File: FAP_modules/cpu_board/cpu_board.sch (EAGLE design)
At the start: 35 parts, among them IC2 74HC245DW, IC3 74HC245DW, IC4 74HC04D, IC7 74HC245DW, IC8 74HC245DW, IC9 74HC245DW

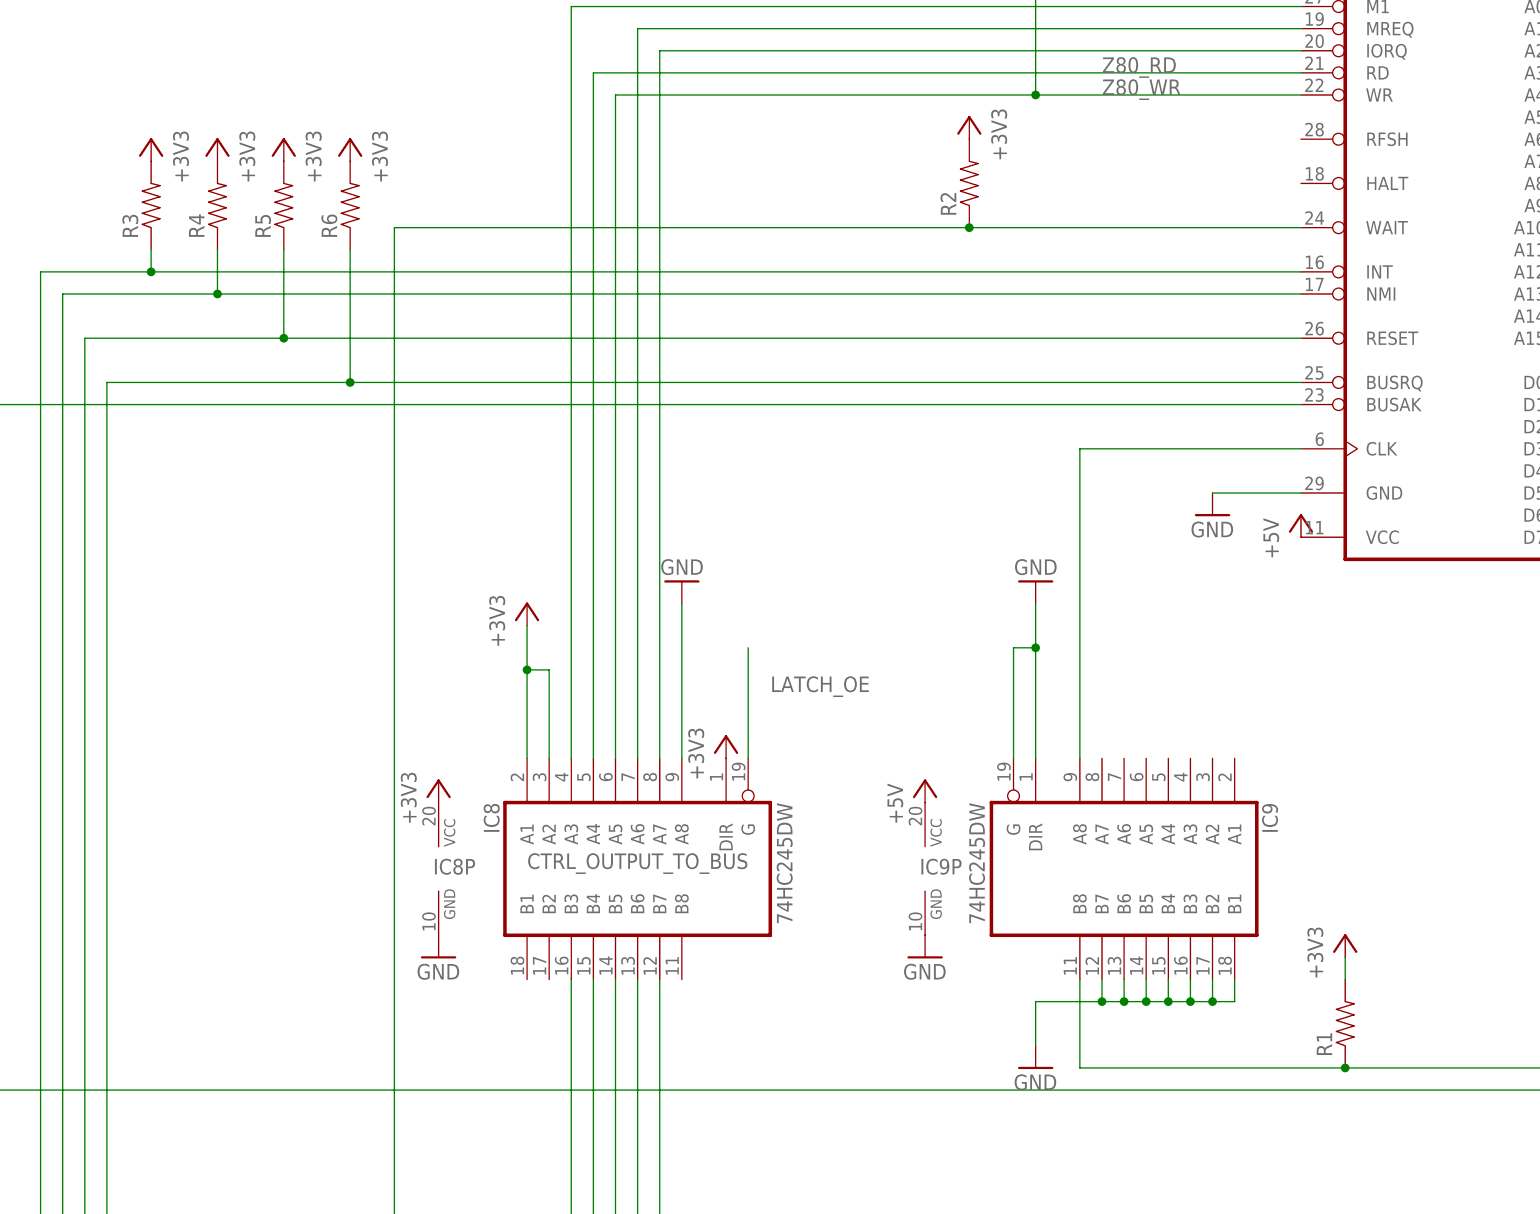
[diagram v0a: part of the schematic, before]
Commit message: new memory board
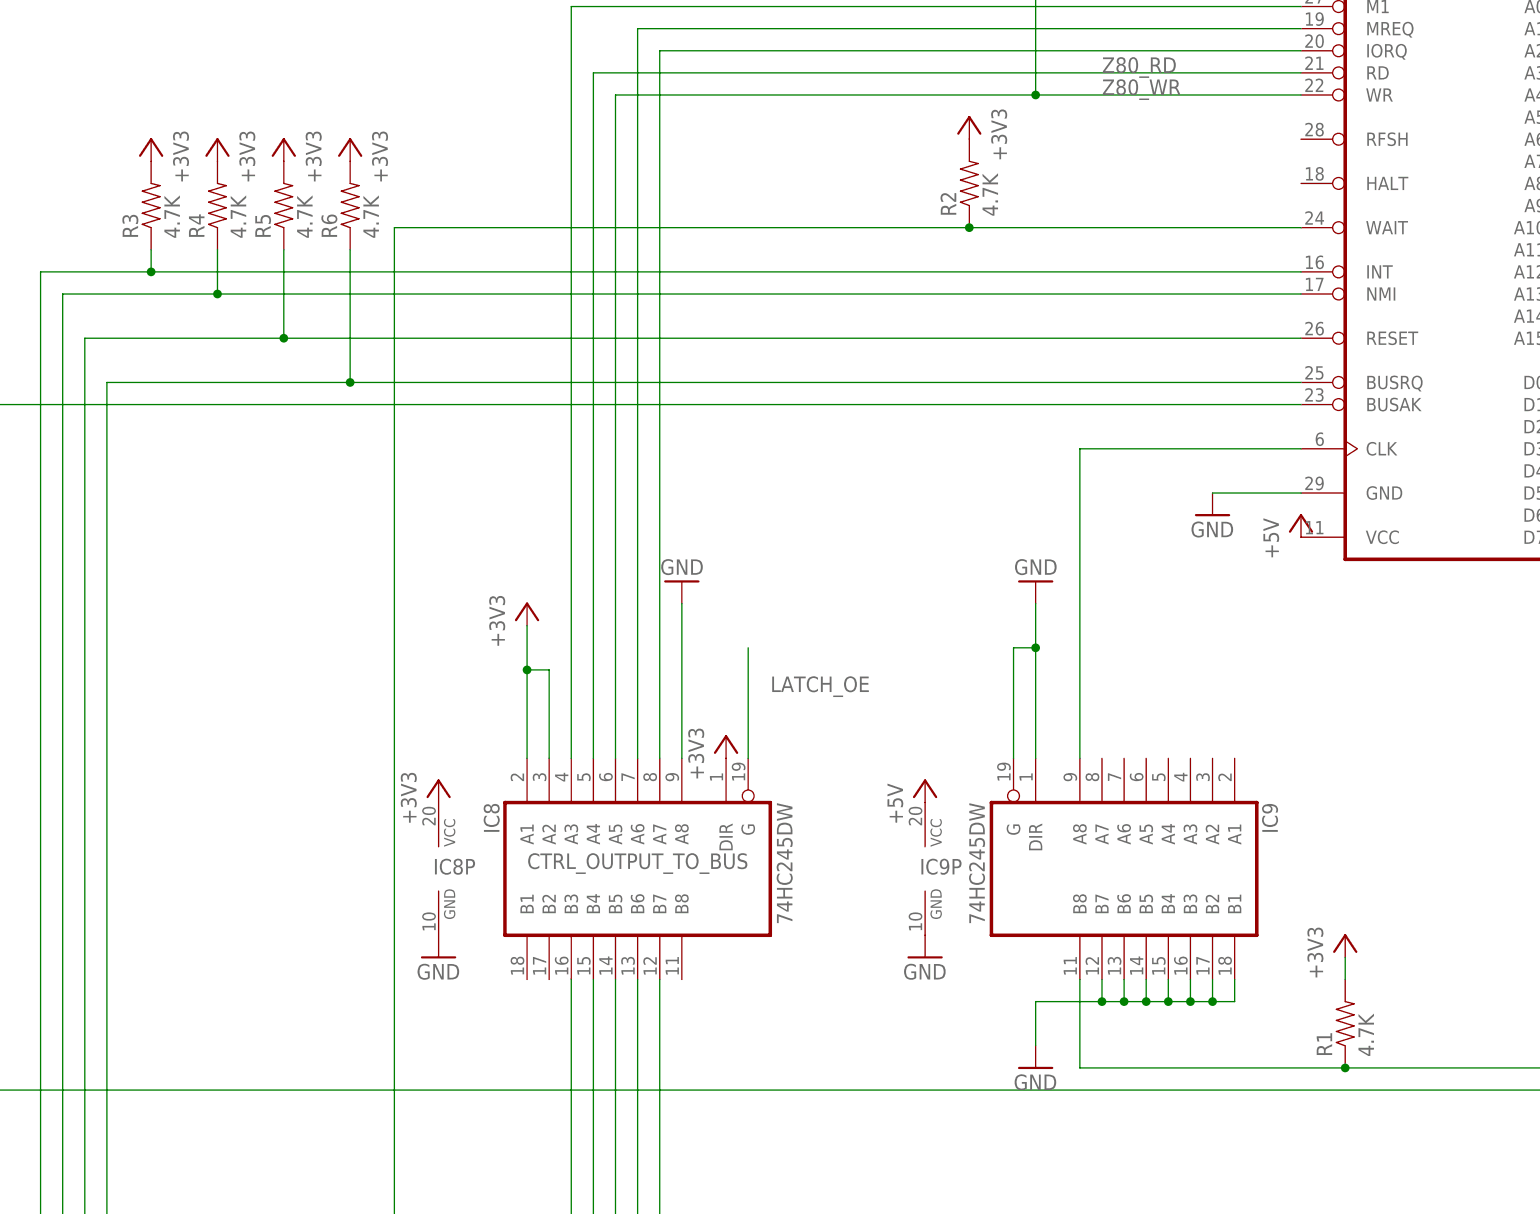
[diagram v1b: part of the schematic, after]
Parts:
- R1, R2, R3, R4, R5, R6: value (none) -> 4.7K
- R7, R8: value 50 -> 2K
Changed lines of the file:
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@@
 <?xml version="1.0" encoding="utf-8"?>
 <!DOCTYPE eagle SYSTEM "eagle.dtd">
-<eagle version="7.6.0">
+<eagle version="7.7.0">
 <drawing>
 <settings>
@@
 <part name="+3V8" library="supply1" deviceset="+3V3" device=""/>
 <part name="+3V9" library="supply1" deviceset="+3V3" device=""/>
-<part name="R3" library="SparkFun-Resistors" deviceset="RESISTOR" device="0805-RES"/>
-<part name="R4" library="SparkFun-Resistors" deviceset="RESISTOR" device="0805-RES"/>
-<part name="R5" library="SparkFun-Resistors" deviceset="RESISTOR" device="0805-RES"/>
-<part name="R6" library="SparkFun-Resistors" deviceset="RESISTOR" device="0805-RES"/>
+<part name="R3" library="SparkFun-Resistors" deviceset="RESISTOR" device="0805-RES" value="4.7K"/>
+<part name="R4" library="SparkFun-Resistors" deviceset="RESISTOR" device="0805-RES" value="4.7K"/>
+<part name="R5" library="SparkFun-Resistors" deviceset="RESISTOR" device="0805-RES" value="4.7K"/>
+<part name="R6" library="SparkFun-Resistors" deviceset="RESISTOR" device="0805-RES" value="4.7K"/>
 <part name="+3V11" library="supply1" deviceset="+3V3" device=""/>
 <part name="+3V12" library="supply1" deviceset="+3V3" device=""/>
@@
 <part name="U$3" library="m3_mounting_hole" deviceset="M3_MOUNTING_HOLE" device=""/>
 <part name="LED2" library="adafruit" deviceset="LED" device="CHIP-LED0805"/>
-<part name="R7" library="SparkFun-Passives" deviceset="RESISTOR" device="0805-RES" value="50"/>
+<part name="R7" library="SparkFun-Passives" deviceset="RESISTOR" device="0805-RES" value="2K"/>
 <part name="LED3" library="adafruit" deviceset="LED" device="CHIP-LED0805"/>
 <part name="GND16" library="supply1" deviceset="GND" device=""/>
-<part name="R8" library="SparkFun-Passives" deviceset="RESISTOR" device="0805-RES" value="50"/>
+<part name="R8" library="SparkFun-Passives" deviceset="RESISTOR" device="0805-RES" value="2K"/>
 <part name="+3V18" library="supply1" deviceset="+3V3" device=""/>
 <part name="GND13" library="supply1" deviceset="GND" device=""/>
@@
 <part name="+3V19" library="supply1" deviceset="+3V3" device=""/>
 <part name="+3V6" library="supply1" deviceset="+3V3" device=""/>
-<part name="R1" library="SparkFun-Resistors" deviceset="RESISTOR" device="0805-RES"/>
+<part name="R1" library="SparkFun-Resistors" deviceset="RESISTOR" device="0805-RES" value="4.7K"/>
 <part name="+3V10" library="supply1" deviceset="+3V3" device=""/>
-<part name="R2" library="SparkFun-Resistors" deviceset="RESISTOR" device="0805-RES"/>
+<part name="R2" library="SparkFun-Resistors" deviceset="RESISTOR" device="0805-RES" value="4.7K"/>
 </parts>
 <sheets>

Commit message: board cleanup
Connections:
- net +3V3: now also IC4A.I, IC4C.I, IC4F.I
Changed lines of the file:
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@@
 <part name="+3V10" library="supply1" deviceset="+3V3" device=""/>
 <part name="R2" library="SparkFun-Resistors" deviceset="RESISTOR" device="0805-RES" value="4.7K"/>
+<part name="+3V15" library="supply1" deviceset="+3V3" device=""/>
+<part name="+3V20" library="supply1" deviceset="+3V3" device=""/>
+<part name="+3V21" library="supply1" deviceset="+3V3" device=""/>
 </parts>
 <sheets>
@@
 <instance part="+3V10" gate="G$1" x="7.62" y="83.82" rot="MR0"/>
 <instance part="R2" gate="G$1" x="7.62" y="76.2" rot="R90"/>
+<instance part="+3V15" gate="G$1" x="-195.58" y="177.8"/>
+<instance part="+3V20" gate="G$1" x="-195.58" y="154.94"/>
+<instance part="+3V21" gate="G$1" x="-195.58" y="127"/>
 </instances>
 <busses>
@@
 <pinref part="R2" gate="G$1" pin="2"/>
 </segment>
+<segment>
+<pinref part="IC4" gate="A" pin="I"/>
+<pinref part="+3V15" gate="G$1" pin="+3V3"/>
+</segment>
+<segment>
+<pinref part="IC4" gate="C" pin="I"/>
+<pinref part="+3V20" gate="G$1" pin="+3V3"/>
+</segment>
+<segment>
+<pinref part="IC4" gate="F" pin="I"/>
+<pinref part="+3V21" gate="G$1" pin="+3V3"/>
+</segment>
 </net>

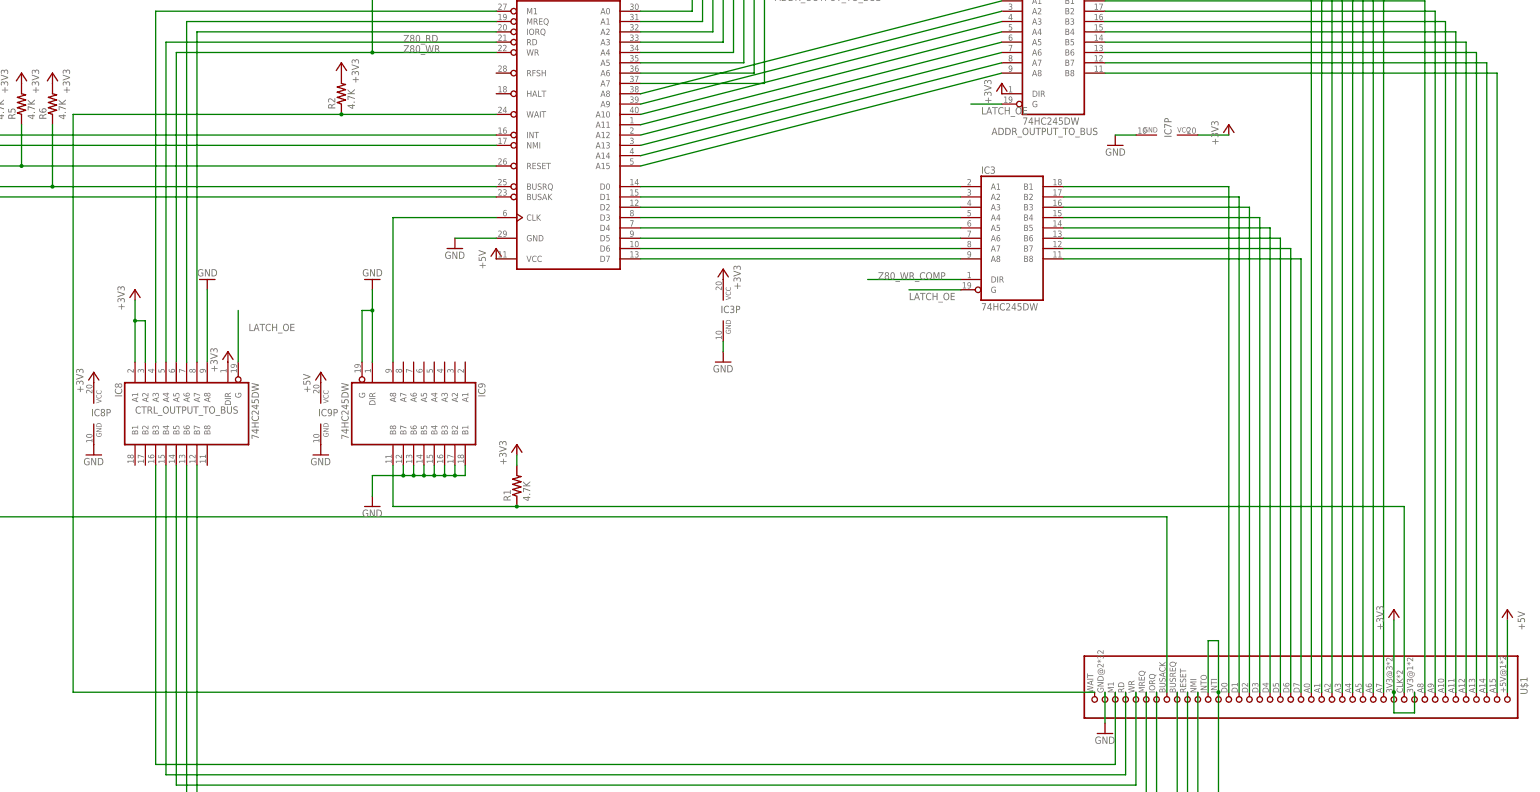
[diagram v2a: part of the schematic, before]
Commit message: added all Z80 signals on bus
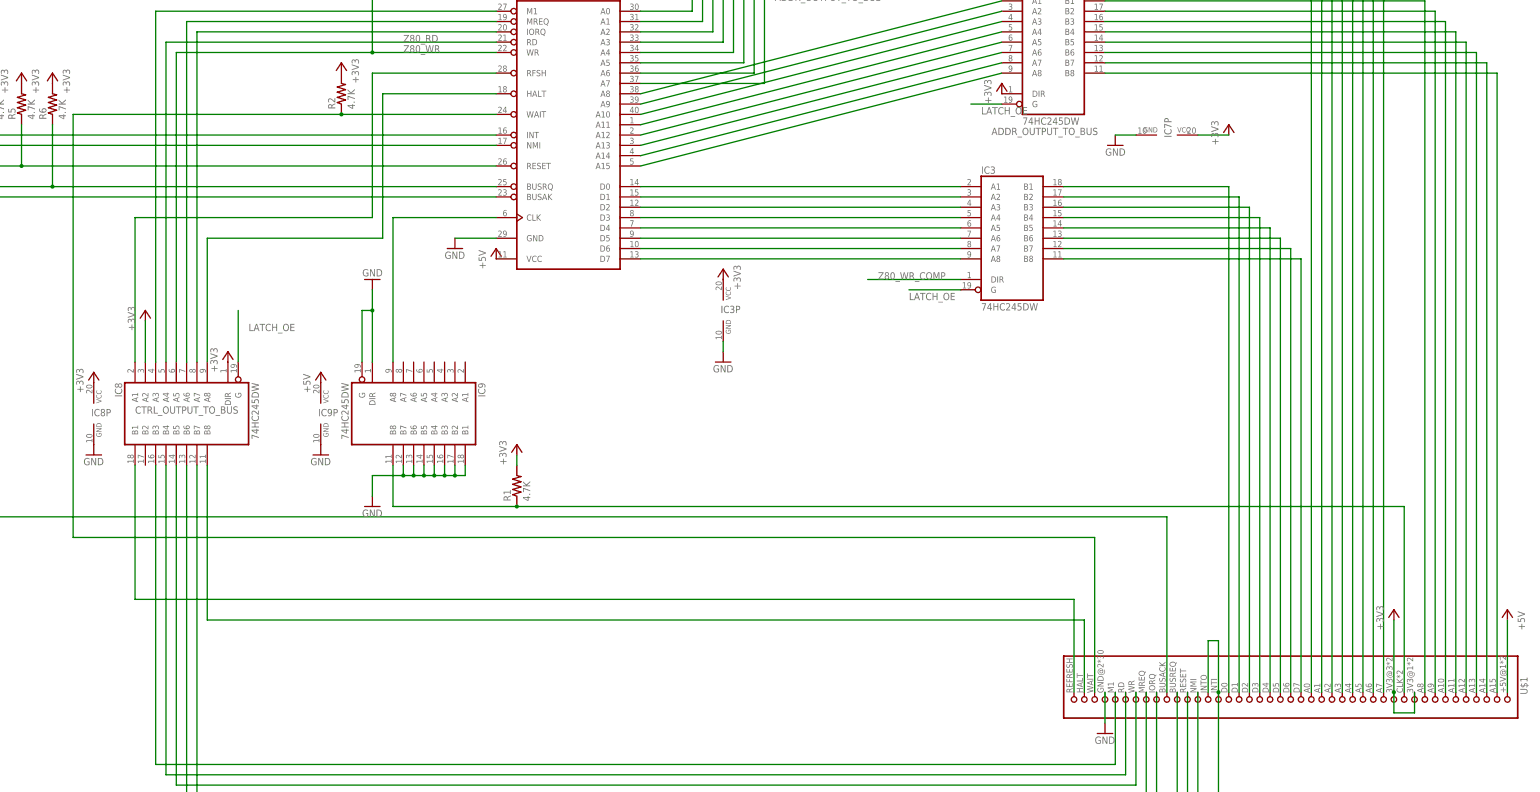
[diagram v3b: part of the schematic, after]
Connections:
- new net N$34: IC1.HALT, IC8A.A8
- new net N$37: IC8A.B8, U$1.41
- new net N$38: IC1.RFSH, IC8A.A1
- new net N$70: IC8A.B1, U$1.42
- net +3V3: no longer IC8A.A1
- net GND: no longer IC8A.A8
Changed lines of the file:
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@@
 <part name="+3V18" library="supply1" deviceset="+3V3" device=""/>
 <part name="GND13" library="supply1" deviceset="GND" device=""/>
-<part name="GND17" library="supply1" deviceset="GND" device=""/>
 <part name="+3V19" library="supply1" deviceset="+3V3" device=""/>
 <part name="+3V6" library="supply1" deviceset="+3V3" device=""/>
@@
 <instance part="IC4" gate="E" x="-154.94" y="50.8" rot="R180"/>
 <instance part="IC4" gate="F" x="-185.42" y="124.46"/>
-<instance part="GND17" gate="1" x="-25.4" y="30.48" rot="R180"/>
-<instance part="+3V19" gate="G$1" x="-43.18" y="27.94"/>
+<instance part="+3V19" gate="G$1" x="-40.64" y="22.86"/>
 <instance part="+3V6" gate="G$1" x="50.8" y="-10.16"/>
 <instance part="R1" gate="G$1" x="50.8" y="-20.32" rot="R90"/>
@@
 <wire x1="-243.84" y1="66.04" x2="-238.76" y2="66.04" width="0.1524" layer="91"/>
 </segment>
-<segment>
-<pinref part="IC8" gate="A" pin="A8"/>
-<pinref part="GND17" gate="1" pin="GND"/>
-<wire x1="-25.4" y1="27.94" x2="-25.4" y2="10.16" width="0.1524" layer="91"/>
-</segment>
 </net>
 <net name="+3V3" class="0">
@@
 </segment>
 <segment>
-<pinref part="IC8" gate="A" pin="A1"/>
-<pinref part="+3V19" gate="G$1" pin="+3V3"/>
-<wire x1="-43.18" y1="25.4" x2="-43.18" y2="20.32" width="0.1524" layer="91"/>
-<pinref part="IC8" gate="A" pin="A2"/>
-<wire x1="-43.18" y1="20.32" x2="-43.18" y2="10.16" width="0.1524" layer="91"/>
-<wire x1="-43.18" y1="20.32" x2="-40.64" y2="20.32" width="0.1524" layer="91"/>
-<wire x1="-40.64" y1="20.32" x2="-40.64" y2="10.16" width="0.1524" layer="91"/>
-<junction x="-43.18" y="20.32"/>
-</segment>
-<segment>
 <pinref part="+3V6" gate="G$1" pin="+3V3"/>
 <pinref part="R1" gate="G$1" pin="2"/>
@@
 <pinref part="IC4" gate="F" pin="I"/>
 <pinref part="+3V21" gate="G$1" pin="+3V3"/>
+</segment>
+<segment>
+<pinref part="IC8" gate="A" pin="A2"/>
+<wire x1="-40.64" y1="20.32" x2="-40.64" y2="10.16" width="0.1524" layer="91"/>
+<pinref part="+3V19" gate="G$1" pin="+3V3"/>
 </segment>
 </net>
@@
 <net name="N$32" class="0">
 <segment>
-<pinref part="U$1" gate="G$1" pin="40"/>
-<wire x1="193.04" y1="-71.12" x2="-58.42" y2="-71.12" width="0.1524" layer="91"/>
-<wire x1="-58.42" y1="-71.12" x2="-58.42" y2="71.12" width="0.1524" layer="91"/>
+<wire x1="-58.42" y1="-33.02" x2="-58.42" y2="71.12" width="0.1524" layer="91"/>
 <wire x1="-58.42" y1="71.12" x2="7.62" y2="71.12" width="0.1524" layer="91"/>
 <pinref part="IC1" gate="1" pin="WAIT"/>
@@
 <wire x1="7.62" y1="71.12" x2="45.72" y2="71.12" width="0.1524" layer="91"/>
 <junction x="7.62" y="71.12"/>
-</segment>
-</net>
+<pinref part="U$1" gate="G$1" pin="40"/>
+<wire x1="193.04" y1="-71.12" x2="193.04" y2="-33.02" width="0.1524" layer="91"/>
+<wire x1="193.04" y1="-33.02" x2="-58.42" y2="-33.02" width="0.1524" layer="91"/>
+</segment>
+</net>
+<net name="N$34" class="0">
+<segment>
+<pinref part="IC1" gate="1" pin="HALT"/>
+<wire x1="45.72" y1="76.2" x2="17.78" y2="76.2" width="0.1524" layer="91"/>
+<wire x1="17.78" y1="76.2" x2="17.78" y2="40.64" width="0.1524" layer="91"/>
+<wire x1="17.78" y1="40.64" x2="-25.4" y2="40.64" width="0.1524" layer="91"/>
+<pinref part="IC8" gate="A" pin="A8"/>
+<wire x1="-25.4" y1="40.64" x2="-25.4" y2="10.16" width="0.1524" layer="91"/>
+</segment>
+</net>
+<net name="N$37" class="0">
+<segment>
+<pinref part="IC8" gate="A" pin="B8"/>
+<wire x1="-25.4" y1="-15.24" x2="-25.4" y2="-53.34" width="0.1524" layer="91"/>
+<wire x1="-25.4" y1="-53.34" x2="190.5" y2="-53.34" width="0.1524" layer="91"/>
+<pinref part="U$1" gate="G$1" pin="41"/>
+<wire x1="190.5" y1="-53.34" x2="190.5" y2="-71.12" width="0.1524" layer="91"/>
+</segment>
+</net>
+<net name="N$38" class="0">
+<segment>
+<pinref part="IC1" gate="1" pin="RFSH"/>
+<wire x1="45.72" y1="81.28" x2="15.24" y2="81.28" width="0.1524" layer="91"/>
+<wire x1="15.24" y1="81.28" x2="15.24" y2="45.72" width="0.1524" layer="91"/>
+<wire x1="15.24" y1="45.72" x2="-43.18" y2="45.72" width="0.1524" layer="91"/>
+<pinref part="IC8" gate="A" pin="A1"/>
+<wire x1="-43.18" y1="45.72" x2="-43.18" y2="10.16" width="0.1524" layer="91"/>
+</segment>
+</net>
+<net name="N$70" class="0">
+<segment>
+<pinref part="IC8" gate="A" pin="B1"/>
+<wire x1="-43.18" y1="-15.24" x2="-43.18" y2="-48.26" width="0.1524" layer="91"/>
+<wire x1="-43.18" y1="-48.26" x2="187.96" y2="-48.26" width="0.1524" layer="91"/>
+<pinref part="U$1" gate="G$1" pin="42"/>
+<wire x1="187.96" y1="-48.26" x2="187.96" y2="-71.12" width="0.1524" layer="91"/>
+</segment>
+</net>
